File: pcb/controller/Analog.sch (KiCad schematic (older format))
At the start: 59 parts, among them J7001 Conn_Coaxial, J7002 Conn_Coaxial, U7001 MCP6561-OT, U7002 TLV3501AIDBVR, U7003 THS4551RGT, U7004 SG3225, U7005 AD9609

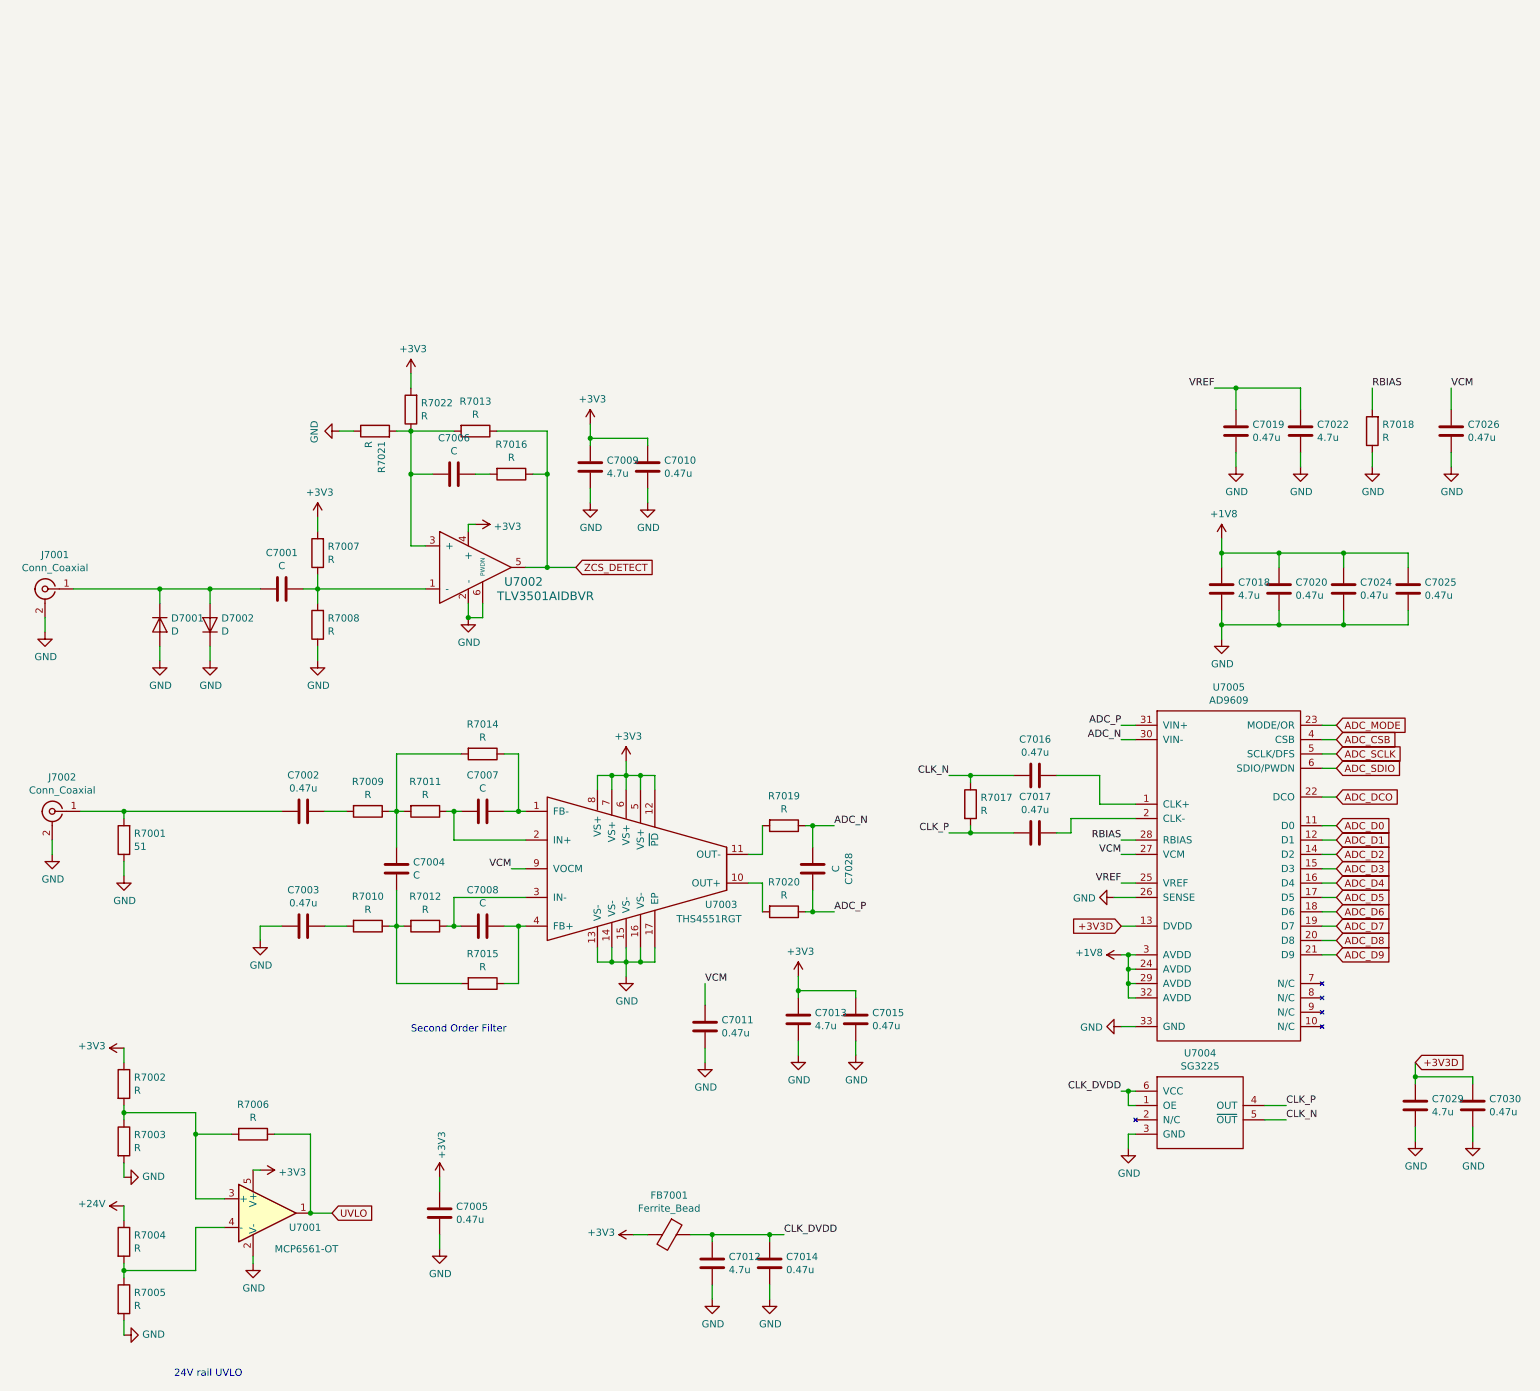
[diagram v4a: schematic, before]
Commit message: updated schematic component values
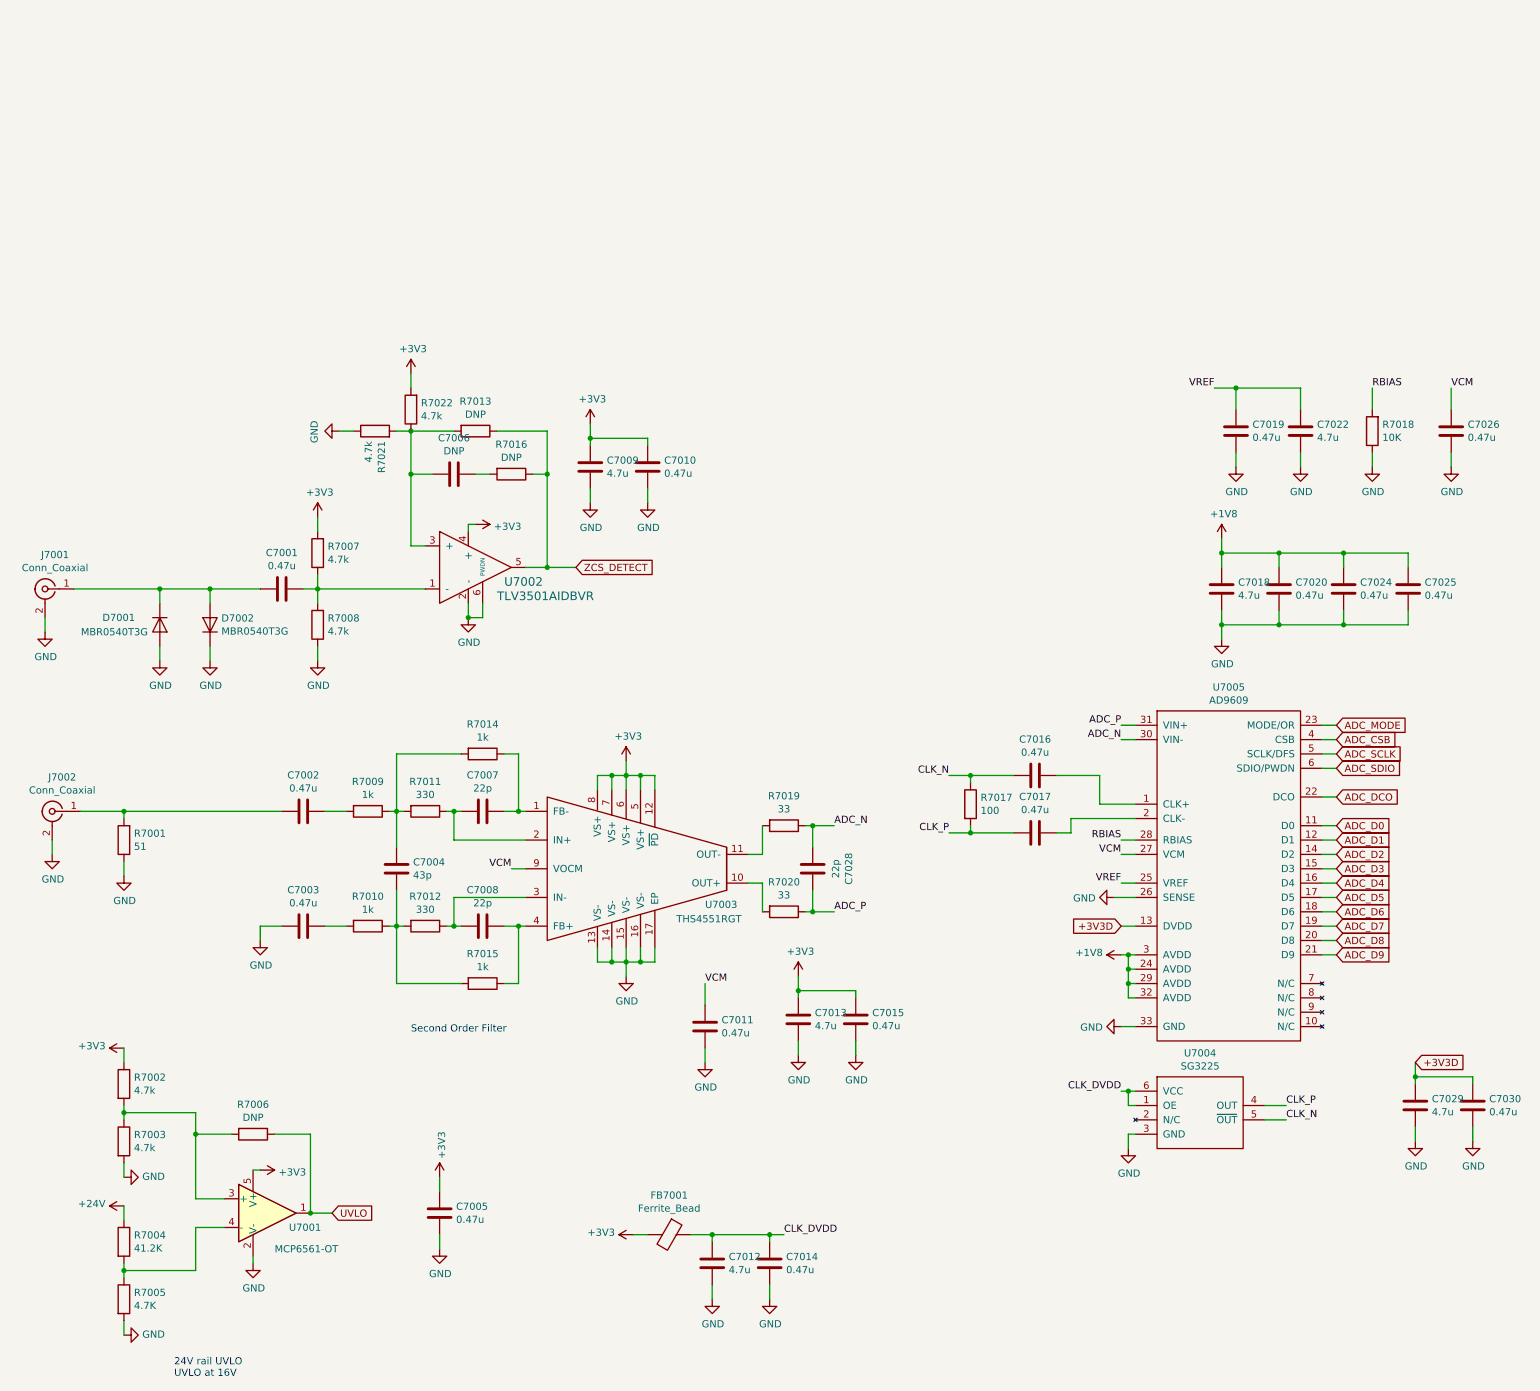
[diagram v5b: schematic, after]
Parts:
- C7001: value C -> 0.47u
- C7004: value C -> 43p
- C7006: value C -> DNP
- C7007, C7008, C7028: value C -> 22p
- D7001, D7002: value D -> MBR0540T3G
- R7002, R7003, R7007, R7008, R7021, R7022: value R -> 4.7k
- R7004: value R -> 41.2K
- R7005: value R -> 4.7K
- R7006, R7013, R7016: value R -> DNP
- R7009, R7010, R7014, R7015: value R -> 1k
- R7011, R7012: value R -> 330
- R7017: value R -> 100
- R7018: value R -> 10K
- R7019, R7020: value R -> 33
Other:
- note added: "24V rail UVLO\nUVLO at 16V"
- note removed: "24V rail UVLO"
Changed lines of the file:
@@
 P 2100 6100
 F 0 "R7006" V 1893 6100 50  0000 C CNN
-F 1 "R" V 1984 6100 50  0000 C CNN
+F 1 "DNP" V 1984 6100 50  0000 C CNN
 F 2 "Resistor_SMD:R_0402_1005Metric" V 2030 6100 50  0001 C CNN
 F 3 "~" H 2100 6100 50  0001 C CNN
@@
 P 1200 5750
 F 0 "R7002" H 1270 5796 50  0000 L CNN
-F 1 "R" H 1270 5705 50  0000 L CNN
+F 1 "4.7k" H 1270 5705 50  0000 L CNN
 F 2 "Resistor_SMD:R_0402_1005Metric" V 1130 5750 50  0001 C CNN
 F 3 "~" H 1200 5750 50  0001 C CNN
@@
 P 1200 6150
 F 0 "R7003" H 1270 6196 50  0000 L CNN
-F 1 "R" H 1270 6105 50  0000 L CNN
+F 1 "4.7k" H 1270 6105 50  0000 L CNN
 F 2 "Resistor_SMD:R_0402_1005Metric" V 1130 6150 50  0001 C CNN
 F 3 "~" H 1200 6150 50  0001 C CNN
@@
 P 1200 6850
 F 0 "R7004" H 1270 6896 50  0000 L CNN
-F 1 "R" H 1270 6805 50  0000 L CNN
+F 1 "41.2K" H 1270 6805 50  0000 L CNN
 F 2 "Resistor_SMD:R_0402_1005Metric" V 1130 6850 50  0001 C CNN
 F 3 "~" H 1200 6850 50  0001 C CNN
@@
 P 1200 7250
 F 0 "R7005" H 1270 7296 50  0000 L CNN
-F 1 "R" H 1270 7205 50  0000 L CNN
+F 1 "4.7K" H 1270 7205 50  0000 L CNN
 F 2 "Resistor_SMD:R_0402_1005Metric" V 1130 7250 50  0001 C CNN
 F 3 "~" H 1200 7250 50  0001 C CNN
@@
 $EndComp
 Text Notes 1550 7800 0    50   ~ 0
-24V rail UVLO
+24V rail UVLO\nUVLO at 16V
 $Comp
 L Device:C C7005
@@
 U 1 1 5C422AC1
 P 1450 2550
-F 0 "D7001" V 1404 2629 50  0000 L CNN
-F 1 "D" V 1495 2629 50  0000 L CNN
+F 0 "D7001" V 1400 2150 50  0000 L CNN
+F 1 "MBR0540T3G" V 1500 2000 50  0000 L CNN
 F 2 "Diode_SMD:D_SOD-123" H 1450 2550 50  0001 C CNN
 F 3 "~" H 1450 2550 50  0001 C CNN
@@
 P 1800 2550
 F 0 "D7002" V 1846 2471 50  0000 R CNN
-F 1 "D" V 1755 2471 50  0000 R CNN
+F 1 "MBR0540T3G" V 1755 2471 50  0000 R CNN
 F 2 "Diode_SMD:D_SOD-123" H 1800 2550 50  0001 C CNN
 F 3 "~" H 1800 2550 50  0001 C CNN
@@
 P 3700 4650
 F 0 "C7008" V 3448 4650 50  0000 C CNN
-F 1 "C" V 3539 4650 50  0000 C CNN
+F 1 "22p" V 3539 4650 50  0000 C CNN
 F 2 "Capacitor_SMD:C_0402_1005Metric" H 3738 4500 50  0001 C CNN
 F 3 "~" H 3700 4650 50  0001 C CNN
@@
 P 3700 5050
 F 0 "R7015" V 3493 5050 50  0000 C CNN
-F 1 "R" V 3584 5050 50  0000 C CNN
+F 1 "1k" V 3584 5050 50  0000 C CNN
 F 2 "Resistor_SMD:R_0402_1005Metric" V 3630 5050 50  0001 C CNN
 F 3 "~" H 3700 5050 50  0001 C CNN
@@
 P 3300 4650
 F 0 "R7012" V 3093 4650 50  0000 C CNN
-F 1 "R" V 3184 4650 50  0000 C CNN
+F 1 "330" V 3184 4650 50  0000 C CNN
 F 2 "Resistor_SMD:R_0402_1005Metric" V 3230 4650 50  0001 C CNN
 F 3 "~" H 3300 4650 50  0001 C CNN
@@
 P 2900 4650
 F 0 "R7010" V 2693 4650 50  0000 C CNN
-F 1 "R" V 2784 4650 50  0000 C CNN
+F 1 "1k" V 2784 4650 50  0000 C CNN
 F 2 "Resistor_SMD:R_0402_1005Metric" V 2830 4650 50  0001 C CNN
 F 3 "~" H 2900 4650 50  0001 C CNN
@@
 P 3100 4250
 F 0 "C7004" H 2985 4204 50  0000 R CNN
-F 1 "C" H 2985 4295 50  0000 R CNN
+F 1 "43p" H 2985 4295 50  0000 R CNN
 F 2 "Capacitor_SMD:C_0402_1005Metric" H 3138 4100 50  0001 C CNN
 F 3 "~" H 3100 4250 50  0001 C CNN
@@
 P 3700 3850
 F 0 "C7007" V 3448 3850 50  0000 C CNN
-F 1 "C" V 3539 3850 50  0000 C CNN
+F 1 "22p" V 3539 3850 50  0000 C CNN
 F 2 "Capacitor_SMD:C_0402_1005Metric" H 3738 3700 50  0001 C CNN
 F 3 "~" H 3700 3850 50  0001 C CNN
@@
 P 3300 3850
 F 0 "R7011" V 3093 3850 50  0000 C CNN
-F 1 "R" V 3184 3850 50  0000 C CNN
+F 1 "330" V 3184 3850 50  0000 C CNN
 F 2 "Resistor_SMD:R_0402_1005Metric" V 3230 3850 50  0001 C CNN
 F 3 "~" H 3300 3850 50  0001 C CNN
@@
 P 3700 3450
 F 0 "R7014" V 3493 3450 50  0000 C CNN
-F 1 "R" V 3584 3450 50  0000 C CNN
+F 1 "1k" V 3584 3450 50  0000 C CNN
 F 2 "Resistor_SMD:R_0402_1005Metric" V 3630 3450 50  0001 C CNN
 F 3 "~" H 3700 3450 50  0001 C CNN
@@
 P 2900 3850
 F 0 "R7009" V 2693 3850 50  0000 C CNN
-F 1 "R" V 2784 3850 50  0000 C CNN
+F 1 "1k" V 2784 3850 50  0000 C CNN
 F 2 "Resistor_SMD:R_0402_1005Metric" V 2830 3850 50  0001 C CNN
 F 3 "~" H 2900 3850 50  0001 C CNN
@@
 P 2300 2300
 F 0 "C7001" V 2048 2300 50  0000 C CNN
-F 1 "C" V 2139 2300 50  0000 C CNN
+F 1 "0.47u" V 2139 2300 50  0000 C CNN
 F 2 "Capacitor_SMD:C_0402_1005Metric" H 2338 2150 50  0001 C CNN
 F 3 "~" H 2300 2300 50  0001 C CNN
@@
 P 2550 2550
 F 0 "R7008" H 2480 2504 50  0000 R CNN
-F 1 "R" H 2480 2595 50  0000 R CNN
+F 1 "4.7k" H 2480 2595 50  0000 R CNN
 F 2 "Resistor_SMD:R_0402_1005Metric" V 2480 2550 50  0001 C CNN
 F 3 "~" H 2550 2550 50  0001 C CNN
@@
 P 2550 2050
 F 0 "R7007" H 2480 2004 50  0000 R CNN
-F 1 "R" H 2480 2095 50  0000 R CNN
+F 1 "4.7k" H 2480 2095 50  0000 R CNN
 F 2 "Resistor_SMD:R_0402_1005Metric" V 2480 2050 50  0001 C CNN
 F 3 "~" H 2550 2050 50  0001 C CNN
@@
 P 3500 1500
 F 0 "C7006" V 3248 1500 50  0000 C CNN
-F 1 "C" V 3339 1500 50  0000 C CNN
+F 1 "DNP" V 3339 1500 50  0000 C CNN
 F 2 "Capacitor_SMD:C_0402_1005Metric" H 3538 1350 50  0001 C CNN
 F 3 "~" H 3500 1500 50  0001 C CNN
@@
 P 3900 1500
 F 0 "R7016" V 3693 1500 50  0000 C CNN
-F 1 "R" V 3784 1500 50  0000 C CNN
+F 1 "DNP" V 3784 1500 50  0000 C CNN
 F 2 "Resistor_SMD:R_0402_1005Metric" V 3830 1500 50  0001 C CNN
 F 3 "~" H 3900 1500 50  0001 C CNN
@@
 P 3650 1200
 F 0 "R7013" V 3443 1200 50  0000 C CNN
-F 1 "R" V 3534 1200 50  0000 C CNN
+F 1 "DNP" V 3534 1200 50  0000 C CNN
 F 2 "Resistor_SMD:R_0402_1005Metric" V 3580 1200 50  0001 C CNN
 F 3 "~" H 3650 1200 50  0001 C CNN
@@
 P 9900 1200
 F 0 "R7018" H 9830 1154 50  0000 R CNN
-F 1 "R" H 9830 1245 50  0000 R CNN
+F 1 "10K" H 9830 1245 50  0000 R CNN
 F 2 "Resistor_SMD:R_0402_1005Metric" V 9830 1200 50  0001 C CNN
 F 3 "~" H 9900 1200 50  0001 C CNN
@@
 P 7100 3800
 F 0 "R7017" H 7170 3846 50  0000 L CNN
-F 1 "R" H 7170 3755 50  0000 L CNN
+F 1 "100" H 7170 3755 50  0000 L CNN
 F 2 "Resistor_SMD:R_0402_1005Metric" V 7030 3800 50  0001 C CNN
 F 3 "~" H 7100 3800 50  0001 C CNN
@@
 P 5800 3950
 F 0 "R7019" V 5593 3950 50  0000 C CNN
-F 1 "R" V 5684 3950 50  0000 C CNN
+F 1 "33" V 5684 3950 50  0000 C CNN
 F 2 "Resistor_SMD:R_0402_1005Metric" V 5730 3950 50  0001 C CNN
 F 3 "~" H 5800 3950 50  0001 C CNN
@@
 P 5800 4550
 F 0 "R7020" V 5593 4550 50  0000 C CNN
-F 1 "R" V 5684 4550 50  0000 C CNN
+F 1 "33" V 5684 4550 50  0000 C CNN
 F 2 "Resistor_SMD:R_0402_1005Metric" V 5730 4550 50  0001 C CNN
 F 3 "~" H 5800 4550 50  0001 C CNN
@@
 P 6000 4250
 F 0 "C7028" V 5748 4250 50  0000 C CNN
-F 1 "C" V 5839 4250 50  0000 C CNN
+F 1 "22p" V 5839 4250 50  0000 C CNN
 F 2 "Capacitor_SMD:C_0402_1005Metric" H 6038 4100 50  0001 C CNN
 F 3 "~" H 6000 4250 50  0001 C CNN
@@
 P 3200 1050
 F 0 "R7022" H 3130 1004 50  0000 R CNN
-F 1 "R" H 3130 1095 50  0000 R CNN
+F 1 "4.7k" H 3130 1095 50  0000 R CNN
 F 2 "Resistor_SMD:R_0402_1005Metric" V 3130 1050 50  0001 C CNN
 F 3 "~" H 3200 1050 50  0001 C CNN
@@
 P 2950 1200
 F 0 "R7021" H 2880 1154 50  0000 R CNN
-F 1 "R" H 2880 1245 50  0000 R CNN
+F 1 "4.7k" H 2880 1245 50  0000 R CNN
 F 2 "Resistor_SMD:R_0402_1005Metric" V 2880 1200 50  0001 C CNN
 F 3 "~" H 2950 1200 50  0001 C CNN
